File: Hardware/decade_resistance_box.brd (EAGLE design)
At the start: 101.6 x 76.2 mm, 61 parts, among them SW1 SWITCH_ROTARY_1X10KIT, SW2 SWITCH_ROTARY_1X10KIT, SW3 SWITCH_ROTARY_1X10KIT, SW4 SWITCH_ROTARY_1X10KIT, SW5 SWITCH_ROTARY_1X10KIT

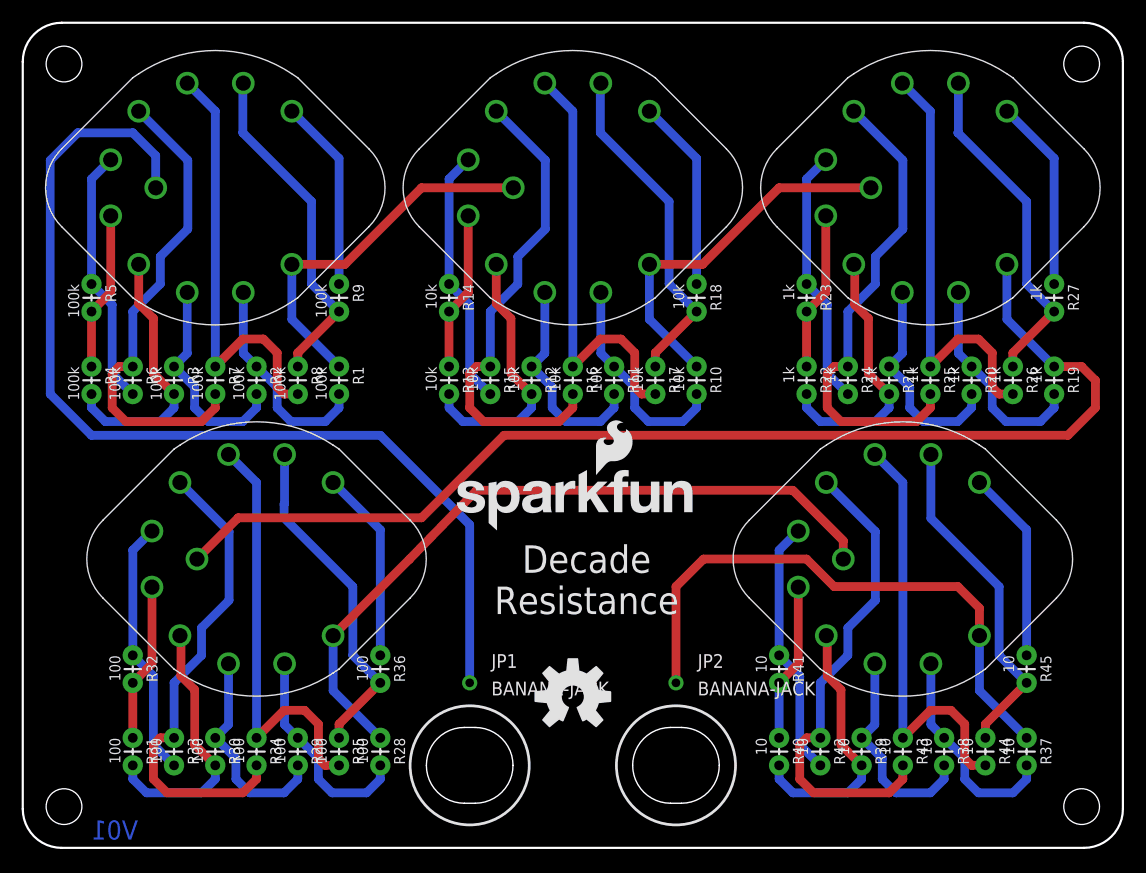
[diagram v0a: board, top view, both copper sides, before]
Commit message: Updated board after review
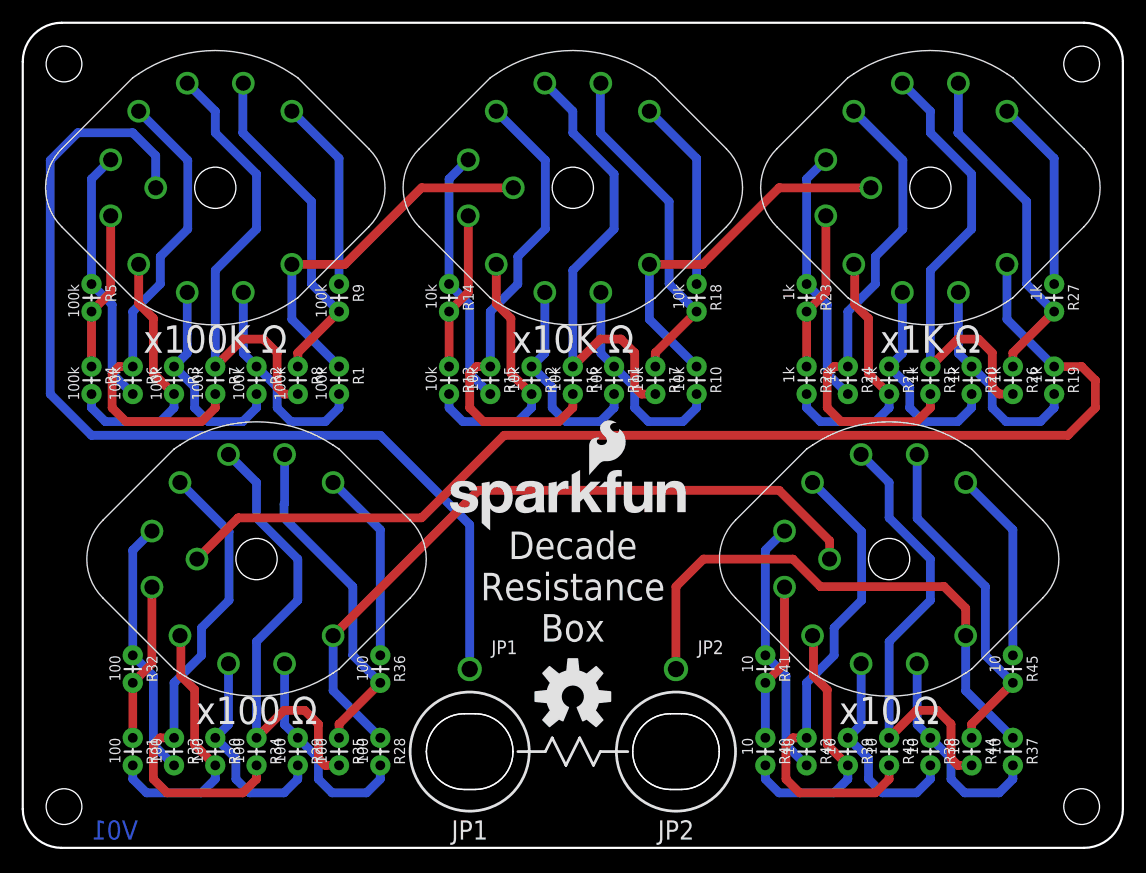
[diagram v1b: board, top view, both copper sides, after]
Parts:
- JP1, JP2: value BANANA-JACK -> (none)
- moved R38 1.27 mm to (83.8, 10.2)
- moved R44 1.27 mm to (87.6, 10.2)
- moved JP1 1.27 mm to (41.3, 8.89)
- moved JP2 1.27 mm to (60.3, 8.89)
- moved R37 1.27 mm to (91.4, 10.2)
- moved R39 1.27 mm to (76.2, 10.2)
- moved R40 1.27 mm to (68.6, 10.2)
- moved R41 1.27 mm to (68.6, 17.8)
- moved R42 1.27 mm to (72.4, 10.2)
- moved R43 1.27 mm to (80.0, 10.2)
- moved R45 1.27 mm to (91.4, 17.8)
- moved SW5 1.27 mm to (80.0, 26.7)
- moved LOGO2 0.63 mm to (38.7, 29.2)
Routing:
- net N$41: track 39.9 -> 43.0 mm
- net N$30: track 39.9 -> 43.0 mm
- net N$19: track 39.9 -> 43.0 mm
- net N$8: track 39.9 -> 43.0 mm
- net N$52: track 39.9 -> 43.0 mm
- net N$45: track 53.6 -> 51.1 mm
- net N$34: track 67.6 -> 66.3 mm
- net N$17: track 94.6 -> 93.3 mm
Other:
- board text added: "Decade Resistance Box"
- board text added: "JP1"
- board text added: "JP2"
- board text added: "x10 Ω"
- board text added: "x100 Ω"
- board text added: "x100K Ω"
- board text added: "x10K Ω"
- board text added: "x1K Ω"
- board text removed: "Decade Resistance"
